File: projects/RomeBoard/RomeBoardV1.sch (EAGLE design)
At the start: 33 parts

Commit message: Package fixes, small updates to schematic
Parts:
- added U$1: LM2576, BrownSpaceEngineering:LM2576

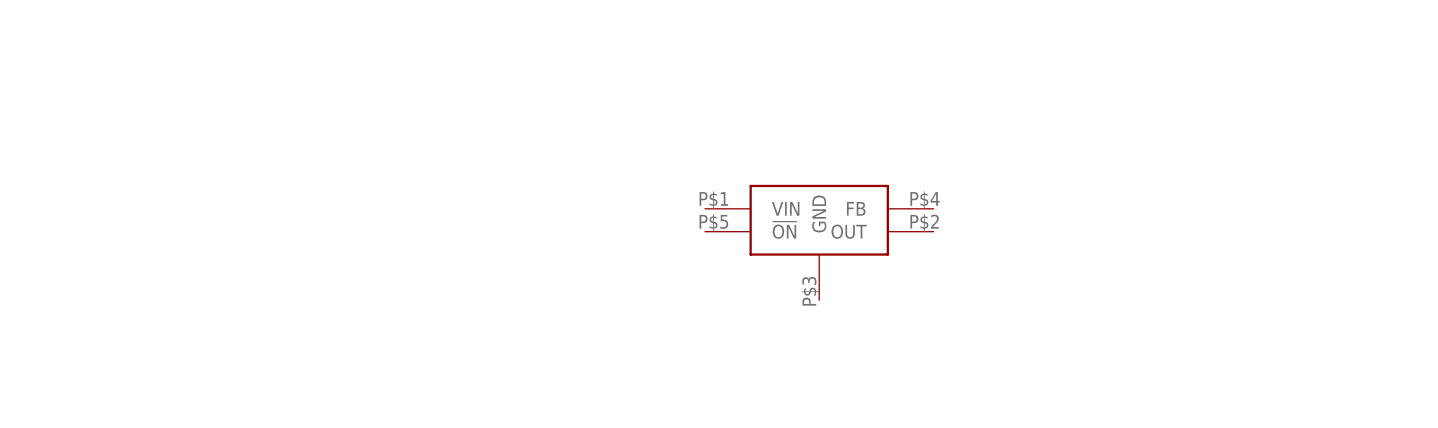
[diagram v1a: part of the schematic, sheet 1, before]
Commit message: 12V->5V regulator
Adding 12V->5V regulator circuit to schematic. All parts added to
library
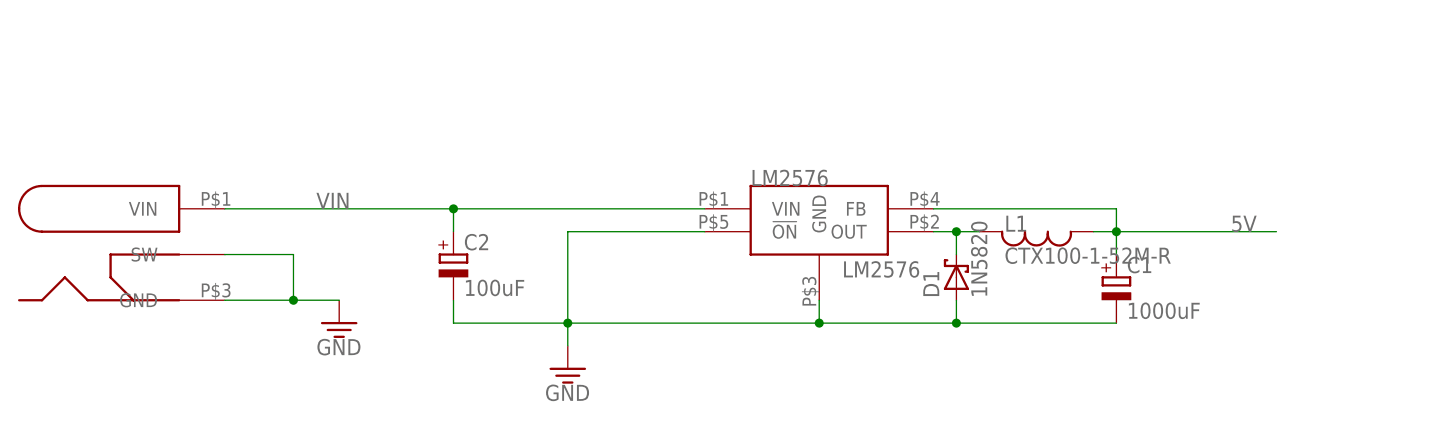
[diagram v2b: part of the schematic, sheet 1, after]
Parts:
- added C1: 1000uF, resistor:CPOL-EUE7.5-16
- added C2: 100uF, resistor:CPOL-EUE3.5-10
- added D1: 1N5820, BrownSpaceEngineering:1N5820
- added L1: CTX100-1-52M-R, BrownSpaceEngineering:CTX100-1-52M-R
- added U$2: PJ-002A, BrownSpaceEngineering:PJ-002A
- renumbered U$1 to LM2576
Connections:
- new net 5V: C1.+, L1.P$2, LM2576.FB
- new net N$1: D1.C, L1.P$1, LM2576.OUT
- net GND: now also C1.-, C2.-, D1.A, LM2576.!ON, LM2576.GND, U$2.GND, U$2.SW
- net VIN: now also C2.+, LM2576.VIN, U$2.VIN
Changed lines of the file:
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@@
 <layer number="18" name="Vias" color="2" fill="1" visible="no" active="no"/>
 <layer number="19" name="Unrouted" color="6" fill="1" visible="no" active="no"/>
-<layer number="20" name="Dimension" color="15" fill="1" visible="no" active="no"/>
+<layer number="20" name="Dimension" color="24" fill="1" visible="no" active="no"/>
 <layer number="21" name="tPlace" color="7" fill="1" visible="no" active="no"/>
 <layer number="22" name="bPlace" color="7" fill="1" visible="no" active="no"/>
@@
 <part name="GND11" library="supply1" deviceset="GND" device=""/>
 <part name="GND12" library="supply1" deviceset="GND" device=""/>
-<part name="U$1" library="BrownSpaceEngineering" deviceset="LM2576" device=""/>
+<part name="U$2" library="BrownSpaceEngineering" deviceset="PJ-002A" device=""/>
+<part name="GND1" library="supply1" deviceset="GND" device=""/>
+<part name="GND2" library="supply1" deviceset="GND" device=""/>
+<part name="C1" library="resistor" deviceset="CPOL-EU" device="E7.5-16" value="1000uF"/>
+<part name="C2" library="resistor" deviceset="CPOL-EU" device="E3.5-10" value="100uF"/>
+<part name="L1" library="BrownSpaceEngineering" deviceset="CTX100-1-52M-R" device=""/>
+<part name="LM2576" library="BrownSpaceEngineering" deviceset="LM2576" device=""/>
+<part name="D1" library="BrownSpaceEngineering" deviceset="1N5820" device=""/>
 </parts>
 <sheets>
@@
 <instance part="GND6" gate="1" x="175.26" y="104.14"/>
 <instance part="GND7" gate="1" x="203.2" y="147.32"/>
-<instance part="U$1" gate="G$1" x="99.06" y="25.4"/>
+<instance part="U$2" gate="G$1" x="20.32" y="22.86"/>
+<instance part="GND1" gate="1" x="45.72" y="15.24"/>
+<instance part="GND2" gate="1" x="71.12" y="10.16"/>
+<instance part="C1" gate="G$1" x="132.08" y="20.32"/>
+<instance part="C2" gate="G$1" x="58.42" y="22.86"/>
+<instance part="L1" gate="G$1" x="121.92" y="25.4"/>
+<instance part="LM2576" gate="G$1" x="99.06" y="25.4"/>
+<instance part="D1" gate="G$1" x="114.3" y="20.32" rot="R90"/>
 </instances>
 <busses>
@@
 <junction x="137.16" y="91.44"/>
 </segment>
+<segment>
+<pinref part="U$2" gate="G$1" pin="SW"/>
+<wire x1="33.02" y1="22.86" x2="40.64" y2="22.86" width="0.1524" layer="91"/>
+<wire x1="40.64" y1="22.86" x2="40.64" y2="17.78" width="0.1524" layer="91"/>
+<pinref part="U$2" gate="G$1" pin="GND"/>
+<wire x1="40.64" y1="17.78" x2="33.02" y2="17.78" width="0.1524" layer="91"/>
+<pinref part="GND1" gate="1" pin="GND"/>
+<wire x1="40.64" y1="17.78" x2="45.72" y2="17.78" width="0.1524" layer="91"/>
+<junction x="40.64" y="17.78"/>
+</segment>
+<segment>
+<wire x1="86.36" y1="25.4" x2="71.12" y2="25.4" width="0.1524" layer="91"/>
+<wire x1="71.12" y1="25.4" x2="71.12" y2="15.24" width="0.1524" layer="91"/>
+<wire x1="99.06" y1="17.78" x2="99.06" y2="15.24" width="0.1524" layer="91"/>
+<wire x1="99.06" y1="15.24" x2="71.12" y2="15.24" width="0.1524" layer="91"/>
+<wire x1="71.12" y1="15.24" x2="71.12" y2="12.7" width="0.1524" layer="91"/>
+<junction x="71.12" y="15.24"/>
+<pinref part="GND2" gate="1" pin="GND"/>
+<pinref part="C2" gate="G$1" pin="-"/>
+<wire x1="58.42" y1="17.78" x2="58.42" y2="15.24" width="0.1524" layer="91"/>
+<wire x1="58.42" y1="15.24" x2="71.12" y2="15.24" width="0.1524" layer="91"/>
+<pinref part="C1" gate="G$1" pin="-"/>
+<wire x1="99.06" y1="15.24" x2="114.3" y2="15.24" width="0.1524" layer="91"/>
+<junction x="99.06" y="15.24"/>
+<pinref part="LM2576" gate="G$1" pin="!ON"/>
+<pinref part="LM2576" gate="G$1" pin="GND"/>
+<pinref part="D1" gate="G$1" pin="A"/>
+<wire x1="114.3" y1="15.24" x2="132.08" y2="15.24" width="0.1524" layer="91"/>
+<wire x1="114.3" y1="17.78" x2="114.3" y2="15.24" width="0.1524" layer="91"/>
+<junction x="114.3" y="15.24"/>
+</segment>
 </net>
 <net name="3V6" class="0">
@@
 <wire x1="96.52" y1="127" x2="91.44" y2="127" width="0.1524" layer="91"/>
 <junction x="96.52" y="127"/>
+</segment>
+<segment>
+<pinref part="U$2" gate="G$1" pin="VIN"/>
+<label x="43.18" y="27.94" size="1.778" layer="95"/>
+<wire x1="33.02" y1="27.94" x2="58.42" y2="27.94" width="0.1524" layer="91"/>
+<pinref part="C2" gate="G$1" pin="+"/>
+<wire x1="58.42" y1="27.94" x2="86.36" y2="27.94" width="0.1524" layer="91"/>
+<wire x1="58.42" y1="25.4" x2="58.42" y2="27.94" width="0.1524" layer="91"/>
+<junction x="58.42" y="27.94"/>
+<pinref part="LM2576" gate="G$1" pin="VIN"/>
 </segment>
 </net>
@@
 </segment>
 </net>
+<net name="N$1" class="0">
+<segment>
+<wire x1="111.76" y1="25.4" x2="114.3" y2="25.4" width="0.1524" layer="91"/>
+<pinref part="L1" gate="G$1" pin="P$1"/>
+<pinref part="LM2576" gate="G$1" pin="OUT"/>
+<pinref part="D1" gate="G$1" pin="C"/>
+<wire x1="114.3" y1="25.4" x2="116.84" y2="25.4" width="0.1524" layer="91"/>
+<wire x1="114.3" y1="22.86" x2="114.3" y2="25.4" width="0.1524" layer="91"/>
+<junction x="114.3" y="25.4"/>
+</segment>
+</net>
+<net name="5V" class="0">
+<segment>
+<wire x1="129.54" y1="25.4" x2="132.08" y2="25.4" width="0.1524" layer="91"/>
+<pinref part="C1" gate="G$1" pin="+"/>
+<wire x1="132.08" y1="25.4" x2="132.08" y2="22.86" width="0.1524" layer="91"/>
+<wire x1="111.76" y1="27.94" x2="132.08" y2="27.94" width="0.1524" layer="91"/>
+<wire x1="132.08" y1="27.94" x2="132.08" y2="25.4" width="0.1524" layer="91"/>
+<junction x="132.08" y="25.4"/>
+<wire x1="132.08" y1="25.4" x2="149.86" y2="25.4" width="0.1524" layer="91"/>
+<label x="144.78" y="25.4" size="1.778" layer="95"/>
+<pinref part="L1" gate="G$1" pin="P$2"/>
+<pinref part="LM2576" gate="G$1" pin="FB"/>
+</segment>
+</net>

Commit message: Adding more parts + moving layout around
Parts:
- removed C14: 680pF, BrownSpaceEngineering:CAP0805
- removed C15: 22pF, BrownSpaceEngineering:CAP0805
- removed C16: 10uF, BrownSpaceEngineering:CAP0805
- removed C17, C18: 100pF, BrownSpaceEngineering:CAP0805
- removed C19: 47uF, BrownSpaceEngineering:CAP0805
- removed C20: 1uF, BrownSpaceEngineering:CAP0805
- removed C21, C22: 0.1uF, BrownSpaceEngineering:CAP0805
- removed C23: 47pF, BrownSpaceEngineering:CAP0805
- removed CNTRLCONN: HARWIN_10_F, CNTRL_BOARD:HARWIN_10_F
- removed L2: 4.7uH, resistor:L-USL3225M
- removed LTC3112: (no value), CNTRL_BOARD:LTC3112
- removed R10: 47K, BrownSpaceEngineering:RES0805
- removed R11: 42.2K, BrownSpaceEngineering:RES0805
- removed R12, R3, R4, R5: 10K, BrownSpaceEngineering:RES0805
- removed R6: 150K, BrownSpaceEngineering:RES0805
- removed R7: 180K, BrownSpaceEngineering:RES0805
- removed R8: 33K, BrownSpaceEngineering:RES0805
- removed R9: 560K, BrownSpaceEngineering:RES0805
- removed V1: VIN, BrownSpaceEngineering:VIA60MIL-SQ
- removed V2: 3V6-SNS, BrownSpaceEngineering:VIA60MIL-SQ
- removed V3: GND, BrownSpaceEngineering:VIA60MIL-SQ
- removed V6: 3V6-EN, BrownSpaceEngineering:VIA60MIL-SQ
- added J2: RASPBERRY-PI-HEADER, BrownSpaceEngineering:RASPBERRY-PI-HEADER
- added R1: 5.76K, passives:RESISTOR-PTH0.4
- added R2: 3K, passives:RESISTOR-PTH0.4
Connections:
- removed net 3V6-EN: CNTRLCONN.7, LTC3112.RUN, V6.P$1
- removed net 3V6-REF: CNTRLCONN.8, R3.2, R4.1
- removed net 3V6-SNS: C18.P$1, CNTRLCONN.3, LTC3112.IOUT, R11.2, V2.P$1
- removed net 5V: C1.+, L1.P$2, LM2576.FB
- removed net COMP: C14.P$2, C15.P$1, LTC3112.COMP
- removed net FB: C15.P$2, LTC3112.FB, R12.1, R6.1, R8.2, R9.2
- removed net N$2: C22.P$2, L2.2, LTC3112.SW1@1, LTC3112.SW1@2
- removed net N$23: C20.P$2, LTC3112.VCC
- removed net N$25: C22.P$1, LTC3112.BST1
- removed net N$28: C21.P$2, L2.1, LTC3112.SW2@1, LTC3112.SW2@2
- removed net N$29: C21.P$1, LTC3112.BST2
- removed net N$4: C14.P$1, R8.1
- removed net N$5: C23.P$2, R12.2
- removed net N$6: R5.1, R6.2
- removed net OVP: C17.P$1, LTC3112.OVP, R10.2, R7.1
- new net N$8: LM2576.FB, R1.1, R2.2
- net 3V6: now also C1.+, L1.P$2, R1.2; no longer C19.P$1, C23.P$1, LTC3112.VOUT, R4.2, R7.2, R9.1
- net GND: now also R2.1; no longer C16.P$2, C17.P$2, C18.P$2, C19.P$2, C20.P$1, CNTRLCONN.2, CNTRLCONN.9, LTC3112.GND, R10.1, R11.1, R3.1, R5.2, V3.P$1
- net P14: no longer CNTRLCONN.4
- net P29: no longer CNTRLCONN.5
- net P3: no longer CNTRLCONN.6
- net VIN: no longer C16.P$1, CNTRLCONN.1, CNTRLCONN.10, LTC3112.PWM/SYNC, LTC3112.VIN@1, LTC3112.VIN@2, V1.P$1
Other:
- moved on the sheet: C1, C2, D1

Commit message: Adding connectors + LED circuits
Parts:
- removed PWR, RET, SEND: LT-T673-Q1R2-25-Z, CNTRL_BOARD:LT-T673-Q1R2-25-Z
- added D2, D3, D4, D5, D6: LEDTHRU-HOLE-CONNECTOR, BrownSpaceEngineering:LEDTHRU-HOLE-CONNECTOR
- added J1: HEADER-5, BrownSpaceEngineering:HEADER-5
- added Q1, Q2, Q3: 2N4401, BrownSpaceEngineering:2N4401
- added R3: 100, passives:RESISTOR-PTH0.4
- added R4: 75, passives:RESISTOR-PTH0.4
- added R5, R6, R7: 89R, passives:RESISTOR-PTH0.4
- V4, V5: device BrownSpaceEngineering:VIA60MIL-SQ -> BrownSpaceEngineering:VIA-120MIL
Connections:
- net P29 renamed !SHDN
- removed net P12: AVX.P$12, PWR.A
- removed net P14: AVX.P$14
- removed net P2: AVX.P$2, SEND.A
- removed net P3: AVX.P$3
- removed net P4: AVX.P$4, RET.A
- new net N$10: D2.C, Q1.1
- new net N$2: D5.A, R3.2
- new net N$3: D6.A, R4.2
- new net N$4: D3.C, Q2.1
- new net N$5: Q1.3, R5.2
- new net N$6: Q2.3, R6.2
- new net N$7: Q3.3, R7.2
- new net N$9: D4.C, Q3.1
- new net PWR_L: AVX.P$12, Q3.2
- new net RX_D: AVX.P$14, J2.P10
- new net RX_L: AVX.P$4, J2.P13, Q2.2
- new net TX_D: AVX.P$3, J2.P8
- new net TX_L: AVX.P$2, J2.P11, Q1.2
- net 3V6: now also R4.1
- net GND: now also D5.C, D6.C, J1.2, J1.3, J1.4, J1.5, J2.P14, J2.P20, J2.P25, J2.P30, J2.P34, J2.P39, J2.P6, J2.P9, R5.1, R6.1, R7.1; no longer PWR.C, RET.C, SEND.C
- net VIN: now also D2.A, D3.A, D4.A, J1.1, R3.1
